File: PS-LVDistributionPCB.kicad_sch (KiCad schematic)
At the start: 2 parts, among them J1 Critical Power, J2 Non-Critical Power

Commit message: finished schematic
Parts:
- removed J1: Critical Power, Connector_Molex:Molex_Sabre_43160-0102_1x02_P7.49mm_Vertical, symbol Connector_Generic:Conn_01x02
- removed J2: Non-Critical Power, Connector_Molex:Molex_Sabre_43160-0102_1x02_P7.49mm_Vertical, symbol Connector_Generic:Conn_01x02
- added F21, F3: 30A, footprints:3588, symbol Device:Fuse
- added J21: CRIT, Connector_Molex:Molex_Sabre_43160-0102_1x02_P7.49mm_Vertical, symbol Connector_Generic:Conn_01x02
- added J5: NON CRIT, Connector_Molex:Molex_Sabre_43160-0102_1x02_P7.49mm_Vertical, symbol Connector_Generic:Conn_01x02
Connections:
- new net: F3.2, J5.1 (Pin_1)
- new net: F21.2, J21.1 (Pin_1)
- new net +12V_CRIT: F21.1
- new net +12V_NON: F3.1
- new net GND: J21.2 (Pin_2), J5.2 (Pin_2)
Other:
- sheet Critical Power Conn renamed Critical Fuses
- sheet Non-Critical Power Conn renamed Non-Critical Fuses
- sheet Critical Fuses ports: added +12V_CRIT; removed none
- sheet Non-Critical Fuses ports: added +12V_NON; removed none

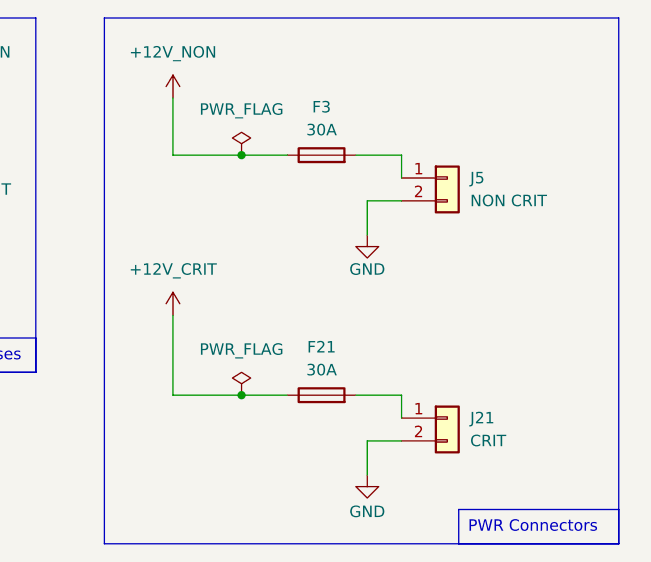
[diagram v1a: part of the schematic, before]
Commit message: rearranged fuses on the back and and connectors on the front for improved waterproofing
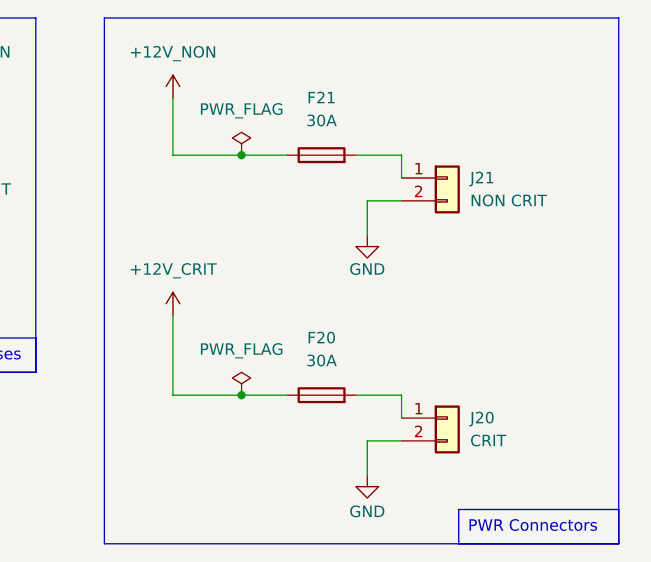
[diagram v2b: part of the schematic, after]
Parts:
- renumbered F21 to F20, F3 to F21, J21 to J20, J5 to J21
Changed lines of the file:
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@@
 		(dnp no)
 		(fields_autoplaced yes)
-		(property "Reference" "J5"
+		(property "Reference" "J21"
 			(at 138.43 48.2599 0)
 			(effects
@@
 			(project "PS-LVDistributionPCB"
 				(path "/bae4e46c-28ae-4193-a5e0-928c081802f5"
-					(reference "J5")
+					(reference "J21")
 					(unit 1)
 				)
@@
 		(dnp no)
 		(fields_autoplaced yes)
-		(property "Reference" "F3"
-			(at 121.92 40.386 90)
+		(property "Reference" "F21"
+			(at 121.92 39.37 90)
 			(effects
 				(font
@@
 		)
 		(property "Value" "30A"
-			(at 121.92 42.926 90)
+			(at 121.92 41.91 90)
 			(effects
 				(font
@@
 			(project "PS-LVDistributionPCB"
 				(path "/bae4e46c-28ae-4193-a5e0-928c081802f5"
-					(reference "F3")
+					(reference "F21")
 					(unit 1)
 				)
@@
 		(dnp no)
 		(fields_autoplaced yes)
-		(property "Reference" "F21"
-			(at 121.92 67.056 90)
+		(property "Reference" "F20"
+			(at 121.92 66.04 90)
 			(effects
 				(font
@@
 		)
 		(property "Value" "30A"
-			(at 121.92 69.596 90)
+			(at 121.92 68.58 90)
 			(effects
 				(font
@@
 			(project "PS-LVDistributionPCB"
 				(path "/bae4e46c-28ae-4193-a5e0-928c081802f5"
-					(reference "F21")
+					(reference "F20")
 					(unit 1)
 				)
@@
 		(dnp no)
 		(fields_autoplaced yes)
-		(property "Reference" "J21"
+		(property "Reference" "J20"
 			(at 138.43 74.9299 0)
 			(effects
@@
 			(project "PS-LVDistributionPCB"
 				(path "/bae4e46c-28ae-4193-a5e0-928c081802f5"
-					(reference "J21")
-					(unit 1)
-				)
+					(reference "J20")
+					(unit 1)
+				)

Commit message: reoriented fuses horizontally to fit enclosure dimensions
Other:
- added sheet Critical Fuses1 (criticalpwr.kicad_sch)
- added sheet Critical Fuses2 (criticalpwr.kicad_sch)
- added sheet Critical Fuses3 (criticalpwr.kicad_sch)
- added sheet Critical Fuses4 (criticalpwr.kicad_sch)
- added sheet Critical Fuses5 (criticalpwr.kicad_sch)
- added sheet Critical Fuses6 (criticalpwr.kicad_sch)
- added sheet Non-Critical Fuses1 (noncriticalpwr.kicad_sch)
- added sheet Non-Critical Fuses10 (noncriticalpwr.kicad_sch)
- added sheet Non-Critical Fuses11 (noncriticalpwr.kicad_sch)
- added sheet Non-Critical Fuses2 (noncriticalpwr.kicad_sch)
- added sheet Non-Critical Fuses3 (noncriticalpwr.kicad_sch)
- added sheet Non-Critical Fuses4 (noncriticalpwr.kicad_sch)
- added sheet Non-Critical Fuses5 (noncriticalpwr.kicad_sch)
- added sheet Non-Critical Fuses6 (noncriticalpwr.kicad_sch)
- added sheet Non-Critical Fuses7 (noncriticalpwr.kicad_sch)
- added sheet Non-Critical Fuses8 (noncriticalpwr.kicad_sch)
- added sheet Non-Critical Fuses9 (noncriticalpwr.kicad_sch)
- sheet Critical Fuses ports: added none; removed +12V_CRIT
- sheet Non-Critical Fuses ports: added none; removed +12V_NON
- note added: "Critical Fuses"
- note added: "Non Critical Fuses"
- moved on the sheet: F20, F21, J20, J21

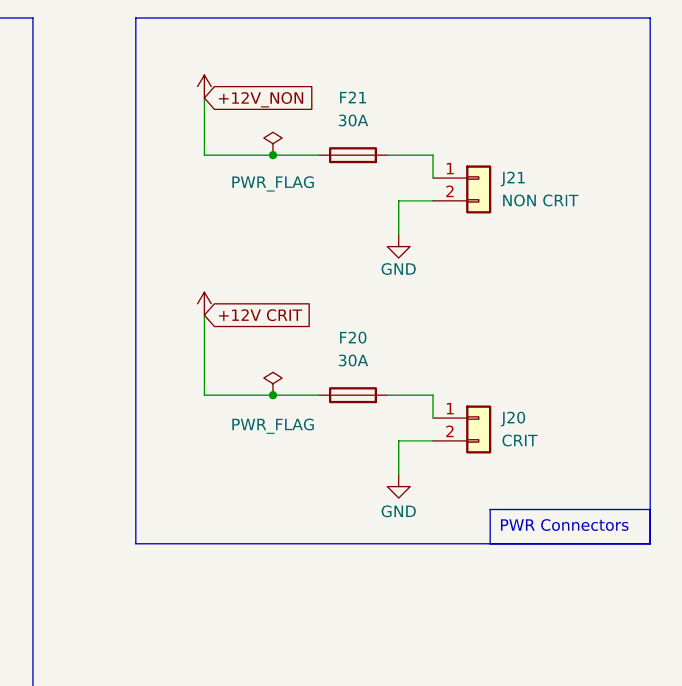
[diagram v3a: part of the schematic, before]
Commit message: Added optoisolators to ensure LED indicators are powered by critical power and only turn on when the fuse blows. Fuses and resistors on the back for waterproofing.
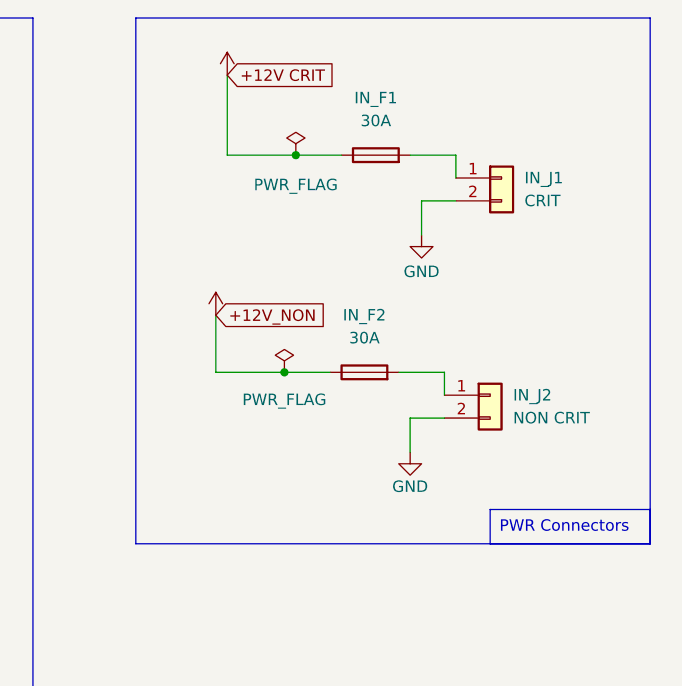
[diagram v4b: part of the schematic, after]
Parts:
- renumbered F20 to IN_F1, F21 to IN_F2, J20 to IN_J1, J21 to IN_J2
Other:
- moved on the sheet: IN_F1, IN_F2, IN_J1, IN_J2

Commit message: solder bridges
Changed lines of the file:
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@@
 (kicad_sch
-	(version 20231120)
+	(version 20250114)
 	(generator "eeschema")
-	(generator_version "8.0")
+	(generator_version "9.0")
 	(paper "A4")
+	(rectangle
+		(start 153.67 120.65)
+		(end 175.26 125.73)
+		(stroke
+			(width 0)
+			(type default)
+		)
+		(fill
+			(type none)
+		)
+	)
+	(rectangle
+		(start 186.69 31.75)
+		(end 243.84 90.17)
+		(stroke
+			(width 0)
+			(type default)
+		)
+		(fill
+			(type none)
+		)
+	)
+	(rectangle
+		(start 49.53 31.75)
+		(end 88.9 139.7)
+		(stroke
+			(width 0)
+			(type default)
+		)
+		(fill
+			(type none)
+		)
+	)
+	(rectangle
+		(start 72.39 134.112)
+		(end 88.9 139.7)
+		(stroke
+			(width 0)
+			(type default)
+		)
+		(fill
+			(type none)
+		)
+	)
+	(rectangle
+		(start 101.6 31.75)
+		(end 175.26 125.73)
+		(stroke
+			(width 0)
+			(type default)
+		)
+		(fill
+			(type none)
+		)
+	)
+	(text "Non Critical Fuses"
+		(exclude_from_sim no)
+		(at 164.338 123.444 0)
+		(effects
+			(font
+				(size 1.27 1.27)
+			)
+		)
+	)
+	(text "Critical Fuses"
+		(exclude_from_sim no)
+		(at 80.772 137.16 0)
+		(effects
+			(font
+				(size 1.27 1.27)
+			)
+		)
+	)
+	(text_box "PWR Connectors"
+		(exclude_from_sim no)
+		(at 226.06 86.36 0)
+		(size 17.78 3.81)
+		(margins 0.9525 0.9525 0.9525 0.9525)
+		(stroke
+			(width 0)
+			(type default)
+		)
+		(fill
+			(type none)
+		)
+		(effects
+			(font
+				(size 1.27 1.27)
+			)
+			(justify left top)
+		)
+	)
 	(junction
 		(at 204.47 46.99)
@@
 			(width 0)
 			(type default)
-		)
-	)
-	(rectangle
-		(start 153.67 120.65)
-		(end 175.26 125.73)
-		(stroke
-			(width 0)
-			(type default)
-		)
-		(fill
-			(type none)
-		)
-	)
-	(rectangle
-		(start 186.69 31.75)
-		(end 243.84 90.17)
-		(stroke
-			(width 0)
-			(type default)
-		)
-		(fill
-			(type none)
-		)
-	)
-	(rectangle
-		(start 49.53 31.75)
-		(end 88.9 139.7)
-		(stroke
-			(width 0)
-			(type default)
-		)
-		(fill
-			(type none)
-		)
-	)
-	(rectangle
-		(start 72.39 134.112)
-		(end 88.9 139.7)
-		(stroke
-			(width 0)
-			(type default)
-		)
-		(fill
-			(type none)
-		)
-	)
-	(rectangle
-		(start 101.6 31.75)
-		(end 175.26 125.73)
-		(stroke
-			(width 0)
-			(type default)
-		)
-		(fill
-			(type none)
-		)
-	)
-	(text_box "PWR Connectors"
-		(exclude_from_sim no)
-		(at 226.06 86.36 0)
-		(size 17.78 3.81)
-		(stroke
-			(width 0)
-			(type default)
-		)
-		(fill
-			(type none)
-		)
-		(effects
-			(font
-				(size 1.27 1.27)
-			)
-			(justify left top)
-		)
-	)
-	(text "Non Critical Fuses"
-		(exclude_from_sim no)
-		(at 164.338 123.444 0)
-		(effects
-			(font
-				(size 1.27 1.27)
-			)
-		)
-	)
-	(text "Critical Fuses"
-		(exclude_from_sim no)
-		(at 80.772 137.16 0)
-		(effects
-			(font
-				(size 1.27 1.27)
-			)
 		)
 	)
@@
 		(at 54.61 80.01)
 		(size 29.21 7.62)
+		(exclude_from_sim no)
+		(in_bom yes)
+		(on_board yes)
+		(dnp no)
 		(fields_autoplaced yes)
 		(stroke
@@
 		(at 140.97 66.04)
 		(size 29.21 7.62)
+		(exclude_from_sim no)
+		(in_bom yes)
+		(on_board yes)
+		(dnp no)
 		(stroke
 			(width 0.1524)
@@
 		(at 106.68 80.01)
 		(size 29.21 7.62)
+		(exclude_from_sim no)
+		(in_bom yes)
+		(on_board yes)
+		(dnp no)
 		(stroke
 			(width 0.1524)
@@
 		(at 54.61 93.98)
 		(size 29.21 7.62)
+		(exclude_from_sim no)
+		(in_bom yes)
+		(on_board yes)
+		(dnp no)
 		(fields_autoplaced yes)
 		(stroke
@@
 		(at 54.61 107.95)
 		(size 29.21 7.62)
+		(exclude_from_sim no)
+		(in_bom yes)
+		(on_board yes)
+		(dnp no)
 		(fields_autoplaced yes)
 		(stroke
@@
 		(at 54.61 66.04)
 		(size 29.21 7.62)
+		(exclude_from_sim no)
+		(in_bom yes)
+		(on_board yes)
+		(dnp no)
 		(fields_autoplaced yes)
 		(stroke
@@
 		(at 140.97 38.1)
 		(size 29.21 7.62)
+		(exclude_from_sim no)
+		(in_bom yes)
+		(on_board yes)
+		(dnp no)
 		(stroke
 			(width 0.1524)
@@
 		(at 140.97 80.01)
 		(size 29.21 7.62)
+		(exclude_from_sim no)
+		(in_bom yes)
+		(on_board yes)
+		(dnp no)
 		(stroke
 			(width 0.1524)
@@
 		(at 106.68 52.07)
 		(size 29.21 7.62)
+		(exclude_from_sim no)
+		(in_bom yes)
+		(on_board yes)
+		(dnp no)
 		(stroke
 			(width 0.1524)
@@
 		(at 140.97 107.95)
 		(size 29.21 7.62)
+		(exclude_from_sim no)
+		(in_bom yes)
+		(on_board yes)
+		(dnp no)
 		(stroke
 			(width 0.1524)
@@
 		(at 140.97 52.07)
 		(size 29.21 7.62)
+		(exclude_from_sim no)
+		(in_bom yes)
+		(on_board yes)
+		(dnp no)
 		(stroke
 			(width 0.1524)
@@
 		(at 54.61 121.92)
 		(size 29.21 7.62)
+		(exclude_from_sim no)
+		(in_bom yes)
+		(on_board yes)
+		(dnp no)
 		(fields_autoplaced yes)
 		(stroke
@@
 		(at 106.68 66.04)
 		(size 29.21 7.62)
+		(exclude_from_sim no)
+		(in_bom yes)
+		(on_board yes)
+		(dnp no)
 		(stroke
 			(width 0.1524)
@@
 		(at 54.61 38.1)
 		(size 29.21 7.62)
+		(exclude_from_sim no)
+		(in_bom yes)
+		(on_board yes)
+		(dnp no)
 		(fields_autoplaced yes)
 		(stroke
@@
 		(at 106.68 107.95)
 		(size 29.21 7.62)
+		(exclude_from_sim no)
+		(in_bom yes)
+		(on_board yes)
+		(dnp no)
 		(stroke
 			(width 0.1524)
@@
 		(at 54.61 52.07)
 		(size 29.21 7.62)
+		(exclude_from_sim no)
+		(in_bom yes)
+		(on_board yes)
+		(dnp no)
 		(fields_autoplaced yes)
 		(stroke
@@
 		(at 106.68 93.98)
 		(size 29.21 7.62)
+		(exclude_from_sim no)
+		(in_bom yes)
+		(on_board yes)
+		(dnp no)
 		(stroke
 			(width 0.1524)
@@
 		(at 106.68 38.1)
 		(size 29.21 7.62)
+		(exclude_from_sim no)
+		(in_bom yes)
+		(on_board yes)
+		(dnp no)
 		(stroke
 			(width 0.1524)
@@
 		(at 140.97 93.98)
 		(size 29.21 7.62)
+		(exclude_from_sim no)
+		(in_bom yes)
+		(on_board yes)
+		(dnp no)
 		(stroke
 			(width 0.1524)
@@
 		)
 	)
+	(embedded_fonts no)
 )
